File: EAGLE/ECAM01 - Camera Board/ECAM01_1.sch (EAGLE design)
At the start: 15 parts, among them J1 DCMI-PRELIM, J2 I2C1-2, Q1 TBD, U1 32F429ZIT6U, U2 IS45S16400J

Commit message: Adding library parts for EBR01, updating schematic
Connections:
- new net ETH_CRS_DV: U1.PA7
- new net ETH_MDC: U1.PC1
- new net ETH_MDIO: U1.PA2
- new net ETH_REF_CLK: U1.PA1
- new net ETH_RXD0: U1.PC4
- new net ETH_RXD1: U1.PC5
- new net ETH_TXD0: U1.PB12
- new net ETH_TXD1: U1.PB13
- new net ETH_TX_EN: U1.PG11

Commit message: Schematic updates, added parts to library for EBR01
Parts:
- added J3: CPL-ETH-MAGJACK-PULSE, TinWhiskers:CPL-ETH-MAGJACK-PULSE
- added R1, R2, R3: 22R, TinWhiskers:CPL-RES-0603-22R-0.1W
- added U3: CPL-ETH-PHY-LAN8720A, TinWhiskers:CPL-ETH-PHY-LAN8720A
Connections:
- new net ETH_RX_ER: U3.10
- new net LED1/REGOFF: U3.3
- new net LED2/NINTSEL: U3.2
- new net N$16: R1.2, U3.8
- new net N$18: R2.2, U3.7
- new net N$19: R3.2, U3.11
- new net NINT/REFCLK0: U3.14
- new net NRST: U3.15
- new net RD+: U3.23
- new net RD-: U3.22
- new net TD+: U3.21
- new net TD-: U3.20
- net ETH_CRS_DV: now also R3.1
- net ETH_MDC: now also U3.13
- net ETH_MDIO: now also U3.12
- net ETH_RXD0: now also R1.1
- net ETH_RXD1: now also R2.1
- net ETH_TXD0: now also U3.17
- net ETH_TXD1: now also U3.18
- net ETH_TX_EN: now also U3.16
- net GND: now also U3.PAD
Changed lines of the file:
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@@
 <part name="DGND2" library="supply1" deviceset="GND" device="" value="DGND"/>
 <part name="FRAME2" library="TinWhiskers" deviceset="A3L-LOC" device=""/>
+<part name="J3" library="TinWhiskers" deviceset="CPL-ETH-MAGJACK-PULSE" device=""/>
+<part name="U3" library="TinWhiskers" deviceset="CPL-ETH-PHY-LAN8720A" device=""/>
+<part name="R1" library="TinWhiskers" deviceset="CPL-RES-0603-22R-0.1W" device="" value="22R"/>
+<part name="R2" library="TinWhiskers" deviceset="CPL-RES-0603-22R-0.1W" device="" value="22R"/>
+<part name="R3" library="TinWhiskers" deviceset="CPL-RES-0603-22R-0.1W" device="" value="22R"/>
+<part name="SUPPLY3" library="TinWhiskers" deviceset="GND" device=""/>
 </parts>
 <sheets>
@@
 <instances>
 <instance part="FRAME2" gate="G$1" x="0" y="0"/>
+<instance part="J3" gate="G$1" x="261.62" y="198.12" smashed="yes">
+<attribute name="NAME" x="284.48" y="208.28" size="1.778" layer="95" font="vector" ratio="12"/>
+</instance>
+<instance part="U3" gate="G$1" x="114.3" y="180.34" smashed="yes">
+<attribute name="NAME" x="137.16" y="210.82" size="1.778" layer="104" font="vector" ratio="12"/>
+</instance>
+<instance part="R1" gate="G$1" x="63.5" y="198.12" smashed="yes">
+<attribute name="NAME" x="59.69" y="199.6186" size="1.778" layer="95"/>
+<attribute name="VALUE" x="59.69" y="194.818" size="1.778" layer="96"/>
+</instance>
+<instance part="R2" gate="G$1" x="63.5" y="190.5" smashed="yes">
+<attribute name="NAME" x="59.69" y="191.9986" size="1.778" layer="95"/>
+<attribute name="VALUE" x="59.69" y="187.198" size="1.778" layer="96"/>
+</instance>
+<instance part="R3" gate="G$1" x="63.5" y="182.88" smashed="yes">
+<attribute name="NAME" x="59.69" y="184.3786" size="1.778" layer="95"/>
+<attribute name="VALUE" x="59.69" y="179.578" size="1.778" layer="96"/>
+</instance>
+<instance part="SUPPLY3" gate="GND" x="106.68" y="170.18"/>
 </instances>
 <busses>
 </busses>
 <nets>
+<net name="ETH_MDC" class="0">
+<segment>
+<pinref part="U3" gate="G$1" pin="13"/>
+<wire x1="96.52" y1="210.82" x2="93.98" y2="210.82" width="0.1524" layer="91"/>
+<label x="93.98" y="210.82" size="1.778" layer="95" rot="R180" xref="yes"/>
+</segment>
+</net>
+<net name="ETH_MDIO" class="0">
+<segment>
+<pinref part="U3" gate="G$1" pin="12"/>
+<wire x1="96.52" y1="213.36" x2="73.66" y2="213.36" width="0.1524" layer="91"/>
+<label x="71.12" y="213.36" size="1.778" layer="95" rot="R180" xref="yes"/>
+<wire x1="73.66" y1="213.36" x2="71.12" y2="213.36" width="0.1524" layer="91"/>
+<wire x1="73.66" y1="213.36" x2="73.66" y2="218.44" width="0.1524" layer="91"/>
+<junction x="73.66" y="213.36"/>
+</segment>
+</net>
+<net name="NINT/REFCLK0" class="0">
+<segment>
+<pinref part="U3" gate="G$1" pin="14"/>
+<wire x1="96.52" y1="208.28" x2="71.12" y2="208.28" width="0.1524" layer="91"/>
+</segment>
+</net>
+<net name="ETH_TXD0" class="0">
+<segment>
+<pinref part="U3" gate="G$1" pin="17"/>
+<wire x1="96.52" y1="205.74" x2="93.98" y2="205.74" width="0.1524" layer="91"/>
+<label x="93.98" y="205.74" size="1.778" layer="95" rot="R180" xref="yes"/>
+</segment>
+</net>
+<net name="ETH_TXD1" class="0">
+<segment>
+<pinref part="U3" gate="G$1" pin="18"/>
+<wire x1="96.52" y1="203.2" x2="68.58" y2="203.2" width="0.1524" layer="91"/>
+<label x="68.58" y="203.2" size="1.778" layer="95" rot="R180" xref="yes"/>
+</segment>
+</net>
+<net name="ETH_TX_EN" class="0">
+<segment>
+<pinref part="U3" gate="G$1" pin="16"/>
+<wire x1="96.52" y1="200.66" x2="93.98" y2="200.66" width="0.1524" layer="91"/>
+<label x="93.98" y="200.66" size="1.778" layer="95" rot="R180" xref="yes"/>
+</segment>
+</net>
+<net name="N$16" class="0">
+<segment>
+<pinref part="U3" gate="G$1" pin="8"/>
+<pinref part="R1" gate="G$1" pin="2"/>
+<wire x1="96.52" y1="198.12" x2="68.58" y2="198.12" width="0.1524" layer="91"/>
+</segment>
+</net>
+<net name="ETH_RXD0" class="0">
+<segment>
+<pinref part="R1" gate="G$1" pin="1"/>
+<wire x1="58.42" y1="198.12" x2="55.88" y2="198.12" width="0.1524" layer="91"/>
+<label x="55.88" y="198.12" size="1.778" layer="95" rot="R180" xref="yes"/>
+</segment>
+</net>
+<net name="N$18" class="0">
+<segment>
+<pinref part="U3" gate="G$1" pin="7"/>
+<wire x1="96.52" y1="195.58" x2="71.12" y2="195.58" width="0.1524" layer="91"/>
+<wire x1="71.12" y1="195.58" x2="71.12" y2="190.5" width="0.1524" layer="91"/>
+<pinref part="R2" gate="G$1" pin="2"/>
+<wire x1="71.12" y1="190.5" x2="68.58" y2="190.5" width="0.1524" layer="91"/>
+</segment>
+</net>
+<net name="N$19" class="0">
+<segment>
+<pinref part="U3" gate="G$1" pin="11"/>
+<wire x1="96.52" y1="193.04" x2="73.66" y2="193.04" width="0.1524" layer="91"/>
+<wire x1="73.66" y1="193.04" x2="73.66" y2="182.88" width="0.1524" layer="91"/>
+<pinref part="R3" gate="G$1" pin="2"/>
+<wire x1="73.66" y1="182.88" x2="68.58" y2="182.88" width="0.1524" layer="91"/>
+</segment>
+</net>
+<net name="ETH_RXD1" class="0">
+<segment>
+<pinref part="R2" gate="G$1" pin="1"/>
+<wire x1="58.42" y1="190.5" x2="55.88" y2="190.5" width="0.1524" layer="91"/>
+<label x="55.88" y="190.5" size="1.778" layer="95" rot="R180" xref="yes"/>
+</segment>
+</net>
+<net name="ETH_CRS_DV" class="0">
+<segment>
+<pinref part="R3" gate="G$1" pin="1"/>
+<wire x1="58.42" y1="182.88" x2="55.88" y2="182.88" width="0.1524" layer="91"/>
+<label x="55.88" y="182.88" size="1.778" layer="95" rot="R180" xref="yes"/>
+</segment>
+</net>
+<net name="ETH_RX_ER" class="0">
+<segment>
+<pinref part="U3" gate="G$1" pin="10"/>
+<wire x1="96.52" y1="190.5" x2="91.44" y2="190.5" width="0.1524" layer="91"/>
+</segment>
+</net>
+<net name="LED1/REGOFF" class="0">
+<segment>
+<pinref part="U3" gate="G$1" pin="3"/>
+<wire x1="96.52" y1="187.96" x2="76.2" y2="187.96" width="0.1524" layer="91"/>
+<wire x1="76.2" y1="187.96" x2="76.2" y2="177.8" width="0.1524" layer="91"/>
+<wire x1="76.2" y1="177.8" x2="53.34" y2="177.8" width="0.1524" layer="91"/>
+<label x="53.34" y="177.8" size="1.778" layer="95" rot="R180" xref="yes"/>
+</segment>
+</net>
+<net name="LED2/NINTSEL" class="0">
+<segment>
+<pinref part="U3" gate="G$1" pin="2"/>
+<wire x1="96.52" y1="185.42" x2="78.74" y2="185.42" width="0.1524" layer="91"/>
+<wire x1="78.74" y1="185.42" x2="78.74" y2="175.26" width="0.1524" layer="91"/>
+<wire x1="78.74" y1="175.26" x2="76.2" y2="175.26" width="0.1524" layer="91"/>
+<label x="76.2" y="175.26" size="1.778" layer="95" rot="R180" xref="yes"/>
+</segment>
+</net>
+<net name="NRST" class="0">
+<segment>
+<pinref part="U3" gate="G$1" pin="15"/>
+<wire x1="96.52" y1="182.88" x2="81.28" y2="182.88" width="0.1524" layer="91"/>
+<wire x1="81.28" y1="182.88" x2="81.28" y2="172.72" width="0.1524" layer="91"/>
+<wire x1="81.28" y1="172.72" x2="55.88" y2="172.72" width="0.1524" layer="91"/>
+<label x="55.88" y="172.72" size="1.778" layer="95" rot="R180" xref="yes"/>
+</segment>
+</net>
+<net name="GND" class="0">
+<segment>
+<pinref part="U3" gate="G$1" pin="PAD"/>
+<pinref part="SUPPLY3" gate="GND" pin="GND"/>
+<wire x1="106.68" y1="172.72" x2="106.68" y2="175.26" width="0.1524" layer="91"/>
+</segment>
+</net>
+<net name="TD+" class="0">
+<segment>
+<pinref part="U3" gate="G$1" pin="21"/>
+<wire x1="129.54" y1="205.74" x2="139.7" y2="205.74" width="0.1524" layer="91"/>
+</segment>
+</net>
+<net name="TD-" class="0">
+<segment>
+<pinref part="U3" gate="G$1" pin="20"/>
+<wire x1="129.54" y1="200.66" x2="139.7" y2="200.66" width="0.1524" layer="91"/>
+</segment>
+</net>
+<net name="RD+" class="0">
+<segment>
+<pinref part="U3" gate="G$1" pin="23"/>
+<wire x1="129.54" y1="193.04" x2="139.7" y2="193.04" width="0.1524" layer="91"/>
+</segment>
+</net>
+<net name="RD-" class="0">
+<segment>
+<pinref part="U3" gate="G$1" pin="22"/>
+<wire x1="129.54" y1="187.96" x2="139.7" y2="187.96" width="0.1524" layer="91"/>
+</segment>
+</net>
 </nets>
 </sheet>

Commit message: Added all necessary library parts for Ethernet circuit, USART1, USART2. Finished schematic capture of Ethernet circuit, USART1, USART2.
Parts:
- added C10, C9: 12pF, TinWhiskers:CPL-CAP-C0G-0603-12PF-50V
- added C11: 0.1uF, TinWhiskers:CPL-CAP-X5R-0603-0.1UF-35V
- added C12, C17: 10uF, TinWhiskers:CPL-CAP-ALU-RAD-10UF-50V
- added C13, C14, C18, C19, C20: 0.1uF, TinWhiskers:CPL-CAP-X7R-0603-0.1UF-35V
- added C15: 1uF, TinWhiskers:CPL-CAP-ALU-SMD-1UF-50V
- added C16: 470pF, TinWhiskers:CPL-CAP-X7R-0603-470PF-100V
- added C21, C22, C23, C24: 18pF, TinWhiskers:CPL-CAP-C0G-0603-18PF-50V
- added FB1: BLM15H0603, TinWhiskers:BLM15H0603
- added J4: USART1, TinWhiskers:CPL-CON-HEADER-0.1IN-2P-M
- added J5: USART2, TinWhiskers:CPL-CON-HEADER-0.1IN-4P-M
- added Q2: 25MHz, TinWhiskers:CPL-OSC-CRY-25MHZ-18PF
- added R10, R11, R12, R13: 49R9, TinWhiskers:CPL-RES-0603-49.9-0.1W
- added R5: 1M, TinWhiskers:CPL-RES-0603-1M-0.1W
- added R6: 12.1K, TinWhiskers:CPL-RES-0603-12.1K-0.1W
- added R7: 22R, TinWhiskers:CPL-RES-0603-22R-0.1W
- added R8: 1.5K, TinWhiskers:CPL-RES-0603-1.5K-50V
- added R9: 10K, TinWhiskers:CPL-RES-0603-10K-0.1W
- added U4: 74LVC1G04, TinWhiskers:CPL-INV-SOT25-5.5V-3.3V
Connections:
- removed net LED2/NINTSEL: U3.2
- new net +3V3: C11.2, C17.POS, C18.2, FB1.1, R8.2, R9.2, U3.9, U4.5
- new net N$21: R7.2, U4.4
- new net N$22: C12.POS, C13.2, C14.2, C19.2, C20.2, FB1.2, J3.4, J3.5, R10.2, R11.2, R12.2, R13.2, U3.1, U3.19
- new net N$23: C15.POS, C16.2, U3.6
- new net RBIAS: R6.2, U3.24
- new net USART1_RX: J4.2, U1.PA10
- new net USART1_TX: J4.1, U1.PA9
- new net USART2_CTS: J5.1, U1.PA0
- new net USART2_RTS: J5.3, U1.PD4
- new net USART2_RX: J5.2, U1.PA3
- new net USART2_TX: J5.4, U1.PD5
- new net XTAL1: C9.2, Q2.1, R5.1, U3.5
- new net XTAL2: C10.2, Q2.2, R5.2, U3.4
- net ETH_MDIO: now also R8.1
- net ETH_REF_CLK: now also R7.1
- net ETH_RX_ER: now also R9.1; no longer U3.10
- net GND: now also C10.1, C11.1, C12.NEG, C13.1, C14.1, C15.NEG, C16.1, C17.NEG, C18.1, C19.1, C20.1, C21.1, C22.1, C23.1, C24.1, C9.1, J3.8, J3.SHLD0, J3.SHLD1, R6.1, U4.3
- net NINT/REFCLK0: now also U4.2
- net RD+: now also C23.2, J3.3, R12.1
- net RD-: now also C24.2, J3.6, R13.1
- net TD+: now also C21.2, J3.1, R10.1
- net TD-: now also C22.2, J3.2, R11.1

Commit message: Trace widths for motor lines increased to handle 2A current. Eliminated/approved all DRC errors except those for Q1, which remain for review by Neil. Refined DRC check to reflect manufacturing specs for HQPCB. The new DRC file will be saved in FPD-Electronics repo ASAP. Board is ready for Gerber export. ECAM01 schematic added connections for pending USB OTG component.
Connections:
- new net USB_OTG_DM: U1.PB14
- new net USB_OTG_DP: U1.PB15
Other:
- moved on the sheet: C1, C2, C3, C4, C5, C6, C7, C8

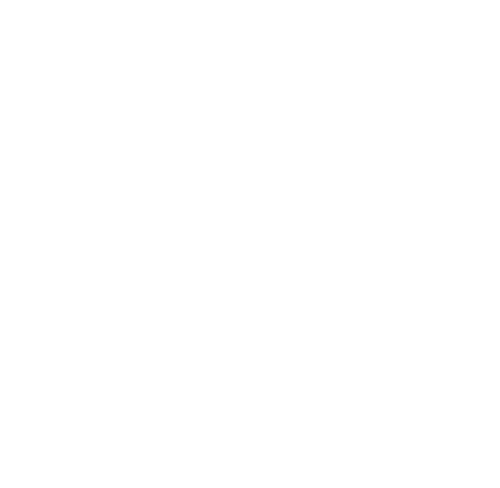
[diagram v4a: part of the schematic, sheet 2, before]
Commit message: Added parts to library for USB_OTG connection.
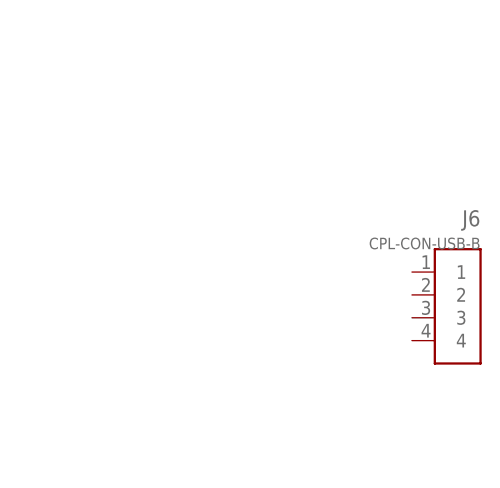
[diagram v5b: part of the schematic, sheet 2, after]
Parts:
- added J6: CPL-CON-USB-B, TinWhiskers:CPL-CON-USB-B
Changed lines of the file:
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@@
 <setting verticaltext="up"/>
 </settings>
-<grid distance="0.1" unitdist="inch" unit="inch" style="lines" multiple="1" display="yes" altdistance="0.05" altunitdist="inch" altunit="inch"/>
+<grid distance="0.1" unitdist="inch" unit="inch" style="lines" multiple="1" display="no" altdistance="0.01" altunitdist="inch" altunit="inch"/>
 <layers>
 <layer number="1" name="Top" color="4" fill="1" visible="no" active="no"/>
@@
 <part name="J4" library="TinWhiskers" deviceset="CPL-CON-HEADER-0.1IN-2P-M" device="" value="USART1"/>
 <part name="J5" library="TinWhiskers" deviceset="CPL-CON-HEADER-0.1IN-4P-M" device="" value="USART2"/>
+<part name="J6" library="TinWhiskers" deviceset="CPL-CON-USB-B" device=""/>
 </parts>
 <sheets>
@@
 <attribute name="VALUE" x="305.308" y="204.216" size="1.27" layer="96" font="vector" ratio="10"/>
 </instance>
+<instance part="J6" gate="G$1" x="355.6" y="149.86" rot="MR0"/>
 </instances>
 <busses>
